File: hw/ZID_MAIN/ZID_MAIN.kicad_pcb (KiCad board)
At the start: 2 copper layers, 144 parts, among them J1 Conn_01x02_Pin_2.54mm, J10 USB-C PWR ONLY, J2 Conn_02x05_2.54mm, J3 Conn_02x05_2.54mm, J4 Conn_02x05_PINHDR_2.54mm, J5 HDR 1x04 Socket, J6 Conn_02x03_Odd_Even, J7 Conn_01x03, J8 BRK EXP SOCKET, J9 Z80-TARGET, M1 WS-RP2040-Zero, SW1 SW_Push, SW2 SW_DIP_x02, U1 74HCT161, U10 74FCT2245, U11 SST39SF010, U12 AS7C1024B-10J, U13 74FCT541C, U14 74AHCT244, U15 74FCT257T, U16 74HCT166, U17 74HCT166, U18 74LVC245, U19 74LVC125AS, U2 74FCT541C, U20 24LC32, U21 ATF1504AS-44T, U22 74AHCT1G125, U23 74LVC273, U24 74AHCT125, U25 74LVC2G04, U3 74FCT541C, U4 MIC2775, U5 OSC-20MHz, U6 Z80 C20MHz-PLCC, U7 ATF1508AS, U8 74FCT2245, U9 74FCT2245

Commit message: Break exp conn 2x20
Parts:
- added TP7: TestPoint, Connector_PinHeader_2.54mm:PinHeader_1x01_P2.54mm_Vertical, F.Cu at (206.4, -30.0)
- added TP8: TestPoint, Connector_PinHeader_2.54mm:PinHeader_1x01_P2.54mm_Vertical, F.Cu at (206.4, -25.4)
- C34: value 220uF -> 100uF; footprint Capacitor_THT:CP_Radial_D6.3mm_P2.50mm -> Capacitor_SMD:C_1210_3225Metric_Pad1.33x2.70mm_HandSolder
- D12: footprint AES_Library:DO-214AB-AES -> Diode_SMD:D_SOD-523
- J2, J3: footprint Connector_PinHeader_2.54mm:PinHeader_2x05_P2.54mm_Vertical -> AES_Library:PinHeader_2x05_AB-AES
- J8: value BRK EXP SOCKET -> BRK-EXP-UNIT; footprint Connector_PinSocket_2.54mm:PinSocket_1x28_P2.54mm_Vertical -> Connector_PinHeader_2.54mm:PinHeader_2x20_P2.54mm_Vertical
- U25: value 74LVC2G04 -> 74LVC3G04; footprint Package_TO_SOT_SMD:SOT-23-6 -> Package_SO:SSOP-8_2.95x2.8mm_P0.65mm
- moved R6 462.4 mm to (-65.1, -39.4)
- moved R7 462.4 mm to (-60.7, -54.1)
- moved R27 460.9 mm to (-41.0, 43.7)
- moved R28 460.7 mm to (-41.0, 48.8)
- moved R29 460.3 mm to (-40.8, 53.8)
- moved R30 460.1 mm to (-40.8, 58.9)
- moved R14 459.7 mm to (-53.6, -50.8)
- moved R15 459.7 mm to (-53.6, -47.9)
- moved R16 459.7 mm to (-53.6, -44.9)
- moved R18 459.7 mm to (-53.6, -39.0)
- moved U19 453.0 mm to (-73.1, -6.99)
- moved U24 445.5 mm to (-34.5, 54.4), turned to 180 degrees
- moved R26 443.6 mm to (-28.0, 52.3)
- moved R25 442.9 mm to (-28.0, 56.9)
- moved D4 437.6 mm to (-46.3, 56.4), turned to -90 degrees
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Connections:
- D10 pad 2: TRST- -> ZBACK-
- D11 pad 1: ZRFSH- -> TRST-
- D11 pad 2: ZBACK- -> ZRFSH-
- J8 pad 1: GND -> LA1
- J8 pad 10: AEN_CLR- -> LA8
- J8 pad 11: BRKHW_DET- -> LA11
- J8 pad 12: BRK2N_AEQ- -> LA10
- J8 pad 13: LA0 -> LA13
- J8 pad 14: LA1 -> LA12
- J8 pad 15: LA2 -> LA15
- J8 pad 16: LA3 -> LA14
- J8 pad 17: LA4 -> BA_CLK
- J8 pad 18: LA5 -> D7_B
- J8 pad 19: LA6 -> BA_CLR-
- J8 pad 2: +5V -> LA0
- J8 pad 20: LA7 -> unconnected-(J8-ADDO1-Pad20)
- J8 pad 21: LA8 -> AEN_CLK
- J8 pad 22: LA9 -> unconnected-(J8-ADDI2-Pad22)
- J8 pad 23: LA10 -> AEN_CLR-
- J8 pad 24: LA11 -> unconnected-(J8-ADDO2-Pad24)
- J8 pad 25: LA12 -> BRKHW_DET-
- J8 pad 26: LA13 -> unconnected-(J8-ADDI3-Pad26)
- J8 pad 27: LA14 -> BRK2N_AEQ-
- J8 pad 28: LA15 -> unconnected-(J8-ADDO3-Pad28)
- J8 pad 3: D7_B -> LA3
- J8 pad 4: unconnected-(J8-ADDR_DOUT-Pad4) -> LA2
- J8 pad 5: BA_CLK -> LA5
- J8 pad 6: BA_CLR- -> LA4
- J8 pad 7: D7_B -> LA7
- J8 pad 8: unconnected-(J8-AEN_DOUT-Pad8) -> LA6
- J8 pad 9: AEN_CLK -> LA9
- RN1 pad 3: /Main Logic/ZA9 -> /Main Logic/ZA10
- RN1 pad 4: /Main Logic/ZA10 -> /Main Logic/ZA9
- RN1 pad 6: /Main Logic/ZA12 -> /Main Logic/ZA13
- RN1 pad 7: /Main Logic/ZA13 -> /Main Logic/ZA12
- RN1 pad 8: /Main Logic/ZA14 -> /Main Logic/ZA15
- RN1 pad 9: /Main Logic/ZA15 -> /Main Logic/ZA14
- U14 pad 1: /Main Logic/BUSACK_L- -> ZBACK-
- U15 pad 15: /Main Logic/BUSACK_H -> /Main Logic/BUSACK
- U25 pad 2: GND -> /Main Logic/BUSACK
- U25 pad 4: /Main Logic/SPICS2- -> GND
- U25 pad 5: +3.3V -> /Main Logic/SPICS2-
- U25 pad 6: /Main Logic/MINT- -> ZBACK-
- U7 pad 1: /Main Logic/BUSACK_H -> /Main Logic/IO1
- U7 pad 2: /Main Logic/BUSACK_L- -> /Main Logic/IO2
- U8 pad 1: /Main Logic/BUSACK_L- -> ZBACK-
- U9 pad 1: /Main Logic/BUSACK_L- -> ZBACK-

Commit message: PCB comp place #1
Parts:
- JP2: value Jumper_2_Small_Open -> Jumper_2_Small_Open_wsto-AES; footprint Connector_PinHeader_2.00mm:PinHeader_1x02_P2.00mm_Vertical -> Connector_PinHeader_2.00mm:PinHeader_1x03_P2.00mm_Vertical
- moved J8 280.7 mm to (233.9, 26.7), turned to -90 degrees
- moved U12 238.6 mm to (125.0, 76.2)
- moved U11 233.5 mm to (142.2, 67.3)
- moved U2 220.3 mm to (175.9, 34.9), turned to 180 degrees
- moved D5 215.9 mm to (106.0, 119.3), turned to -90 degrees
- moved D6 215.5 mm to (109.0, 119.3), turned to -90 degrees
- moved D7 215.3 mm to (112.0, 119.3), turned to -90 degrees
- moved D8 215.1 mm to (115.1, 119.3), turned to -90 degrees
- moved D9 215.0 mm to (118.1, 119.3), turned to -90 degrees
- moved U10 213.9 mm to (213.8, 88.3), turned to 0 degrees
- moved C15 208.6 mm to (217.5, 144.8)
- moved C17 208.6 mm to (217.5, 149.8)
- moved C19 208.6 mm to (221.5, 134.8)
- moved C21 208.6 mm to (221.5, 139.8)
- moved C23 208.6 mm to (221.5, 144.8)
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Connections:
- JP1 pad 1: TRST- -> unconnected-(JP1-A-Pad1)
- JP1 pad 3: unconnected-(JP1-C-Pad3) -> TRST-
- JP2 pad 1: /Main Logic/_CLK -> unconnected-(JP2-A-Pad1)
- JP2 pad 2: /Main Logic/TCLK -> /Main Logic/_CLK
- RN1 pad 3: /Main Logic/ZA10 -> /Main Logic/ZA9
- RN1 pad 4: /Main Logic/ZA9 -> /Main Logic/ZA10
- RN1 pad 6: /Main Logic/ZA13 -> /Main Logic/ZA12
- RN1 pad 7: /Main Logic/ZA12 -> /Main Logic/ZA13
- RN1 pad 8: /Main Logic/ZA15 -> /Main Logic/ZA14
- RN1 pad 9: /Main Logic/ZA14 -> /Main Logic/ZA15
- U8 pad 11: TA7 -> TA0
- U8 pad 12: TA6 -> TA1
- U8 pad 13: TA5 -> TA2
- U8 pad 14: TA4 -> TA3
- U8 pad 15: TA3 -> TA4
- U8 pad 16: TA2 -> TA5
- U8 pad 17: TA1 -> TA6
- U8 pad 18: TA0 -> TA7
- U8 pad 2: /Main Logic/ZA0 -> /Main Logic/ZA7
- U8 pad 3: /Main Logic/ZA1 -> /Main Logic/ZA6
- U8 pad 4: /Main Logic/ZA2 -> /Main Logic/ZA5
- U8 pad 5: /Main Logic/ZA3 -> /Main Logic/ZA4
- U8 pad 6: /Main Logic/ZA4 -> /Main Logic/ZA3
- U8 pad 7: /Main Logic/ZA5 -> /Main Logic/ZA2
- U8 pad 8: /Main Logic/ZA6 -> /Main Logic/ZA1
- U8 pad 9: /Main Logic/ZA7 -> /Main Logic/ZA0
- U9 pad 11: TA15 -> TA8
- U9 pad 12: TA14 -> TA9
- U9 pad 13: TA13 -> TA10
- U9 pad 14: TA12 -> TA11
- U9 pad 15: TA11 -> TA12
- U9 pad 16: TA10 -> TA13
- U9 pad 17: TA9 -> TA14
- U9 pad 18: TA8 -> TA15
- U9 pad 2: /Main Logic/ZA8 -> /Main Logic/ZA15
- U9 pad 3: /Main Logic/ZA9 -> /Main Logic/ZA14
- U9 pad 4: /Main Logic/ZA10 -> /Main Logic/ZA13
- U9 pad 5: /Main Logic/ZA11 -> /Main Logic/ZA12
- U9 pad 6: /Main Logic/ZA12 -> /Main Logic/ZA11
- U9 pad 7: /Main Logic/ZA13 -> /Main Logic/ZA10
- U9 pad 8: /Main Logic/ZA14 -> /Main Logic/ZA9
- U9 pad 9: /Main Logic/ZA15 -> /Main Logic/ZA8

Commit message: PCB layout 2
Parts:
- removed D1: LED BLUE, LED_THT:LED_D3.0mm
- removed D2: LED YELLOW, LED_THT:LED_D3.0mm
- removed D3: LED RED, LED_THT:LED_D3.0mm
- removed D4: LED ORANGE, LED_THT:LED_D3.0mm
- removed D5, D7: LED GREEN, LED_SMD:LED_0805_2012Metric_Pad1.15x1.40mm_HandSolder
- removed D6, D8: LED YELLOW, LED_SMD:LED_0805_2012Metric_Pad1.15x1.40mm_HandSolder
- removed D9: LED RED, LED_SMD:LED_0805_2012Metric_Pad1.15x1.40mm_HandSolder
- added LED1: LED BLUE, LED_THT:LED_D3.0mm, F.Cu at (233.7, 110.2)
- added LED10: LED ORANGE, LED_THT:LED_D3.0mm, F.Cu at (233.7, 115.3)
- added LED2: LED YELLOW, LED_THT:LED_D3.0mm, F.Cu at (233.7, 105.1)
- added LED3: LED RED, LED_THT:LED_D3.0mm, F.Cu at (233.7, 100.1)
- added LED4: LED ORANGE, LED_THT:LED_D3.0mm, F.Cu at (233.7, 95.0)
- added LED5: LED GREEN, LED_SMD:LED_0805_2012Metric_Pad1.15x1.40mm_HandSolder, F.Cu at (74.5, 97.0)
- added LED6: LED GREEN, LED_SMD:LED_0805_2012Metric_Pad1.15x1.40mm_HandSolder, F.Cu at (74.5, 100.1)
- added LED7: LED YELLOW, LED_SMD:LED_0805_2012Metric_Pad1.15x1.40mm_HandSolder, F.Cu at (74.5, 103.1)
- added LED8: LED YELLOW, LED_SMD:LED_0805_2012Metric_Pad1.15x1.40mm_HandSolder, F.Cu at (74.5, 106.1)
- added LED9: LED RED, LED_SMD:LED_0805_2012Metric_Pad1.15x1.40mm_HandSolder, F.Cu at (74.5, 109.2)
- added R37: 1.2k, Resistor_SMD:R_0805_2012Metric, F.Cu at (224.1, 112.0)
- added U26: 74AHCT1G14, Package_TO_SOT_SMD:SOT-23-5, F.Cu at (217.6, 41.8)
- U25: value 74LVC3G04 -> 74LVC2G04; footprint Package_SO:SSOP-8_2.95x2.8mm_P0.65mm -> Package_TO_SOT_SMD:SOT-23-6
- moved TP1 158.7 mm to (233.0, 119.4)
- moved R27 145.3 mm to (224.0, 109.1), turned to 180 degrees
- moved R30 144.6 mm to (224.0, 93.9), turned to 180 degrees
- moved R28 144.5 mm to (224.0, 104.0), turned to 180 degrees
- moved R29 144.1 mm to (224.0, 98.9), turned to 180 degrees
- moved R17 142.3 mm to (223.6, 114.6), turned to 180 degrees
- moved R26 134.9 mm to (218.8, 105.9), turned to -90 degrees
- moved U22 129.3 mm to (214.9, 112.5), turned to 0 degrees
- moved U24 127.5 mm to (215.2, 98.0), turned to 0 degrees
- moved R25 125.0 mm to (212.0, 105.9), turned to -90 degrees
- moved SPARE1 113.3 mm to (111.8, 93.5)
- moved C17 98.7 mm to (244.8, 55.0)
- moved C25 98.7 mm to (248.8, 55.0)
- moved C30 98.7 mm to (252.8, 47.5)
- moved C33 98.7 mm to (252.8, 55.0)
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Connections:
- RN1 pad 2: /Main Logic/ZA8 -> /Main Logic/ZA12
- RN1 pad 3: /Main Logic/ZA9 -> /Main Logic/ZA11
- RN1 pad 5: /Main Logic/ZA11 -> /Main Logic/ZA9
- RN1 pad 6: /Main Logic/ZA12 -> /Main Logic/ZA13
- RN1 pad 7: /Main Logic/ZA13 -> /Main Logic/ZA8
- U25 pad 2: /Main Logic/BUSACK -> GND
- U25 pad 4: GND -> /Main Logic/SPICS2-
- U25 pad 5: /Main Logic/SPICS2- -> +3.3V
- U25 pad 6: ZBACK- -> /Main Logic/MINT-

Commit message: PCB-Main layout 3
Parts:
- moved TP8 17.0 mm to (157.5, 61.7)
- moved TP7 17.0 mm to (157.5, 69.1)
- moved J2 3.46 mm to (231.7, 44.1)
- moved J3 3.46 mm to (231.7, 31.4)
- moved J9 3.46 mm to (231.7, 72.7)
- moved LED1 3.46 mm to (233.7, 106.7)
- moved LED10 3.46 mm to (233.7, 111.9)
- moved LED2 3.46 mm to (233.7, 101.7)
- moved LED3 3.46 mm to (233.7, 96.6)
- moved LED4 3.46 mm to (233.7, 91.5)
- moved R21 3.30 mm to (216.2, 61.0)
- moved J8 3.12 mm to (211.1, 26.7)
- moved R20 3.12 mm to (176.8, 34.5)
- moved R19 3.12 mm to (179.4, 34.5)
- moved TP1 2.56 mm to (233.7, 116.9)
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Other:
- board outline added: 165.1 x 101.6 mm

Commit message: PCB Main: layout 20250411a
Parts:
- added J11: Conn_01x08, Connector_PinHeader_2.54mm:PinHeader_1x08_P2.54mm_Vertical, F.Cu at (215.6, 83.8)
- LED5, LED6, LED7, LED8, LED9: footprint LED_SMD:LED_0805_2012Metric_Pad1.15x1.40mm_HandSolder -> LED_THT:LED_D3.0mm
- moved SW1 179.5 mm to (232.1, 29.2), turned to -90 degrees
- moved J1 149.8 mm to (218.8, 34.3), turned to 90 degrees
- moved U4 137.8 mm to (212.5, 34.6), turned to 0 degrees
- moved U22 25.2 mm to (223.8, 88.9)
- moved TP1 22.3 mm to (234.0, 94.6)
- moved R17 20.8 mm to (226.4, 94.0)
- moved R26 12.7 mm to (216.1, 118.4)
- moved R25 12.4 mm to (212.3, 118.4)
- moved U24 12.4 mm to (215.5, 110.5)
- moved R33 11.8 mm to (81.0, 111.8)
- moved LED1 10.1 mm to (233.7, 116.8)
- moved LED10 10.1 mm to (233.7, 121.9)
- moved LED2 10.1 mm to (233.7, 111.7)
- moved LED3 10.1 mm to (233.7, 106.7)
- moved LED4 10.1 mm to (233.7, 101.6)
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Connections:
- J1 pad 1: Net-(J1-Pin_1) -> GND
- J1 pad 2: GND -> Net-(J1-Pin_2)
- J8 pad 28: unconnected-(J8-ADDO3-Pad28) -> D7_B
- J8 pad 29: +5V -> TM1-
- J8 pad 30: D7_B -> unconnected-(J8-AEDO1-Pad30)
- J8 pad 31: +5V -> TMREQ-
- J8 pad 33: +5V -> TIORQ-
- J8 pad 35: GND -> TWR-
- J8 pad 37: GND -> TRD-
- J8 pad 38: unconnected-(J8-AEDI3-Pad38) -> GND
- J8 pad 40: unconnected-(J8-AEDO3-Pad40) -> +5V
- SW1 pad 2: Net-(J1-Pin_1) -> Net-(J1-Pin_2)
- U4 pad 4: Net-(J1-Pin_1) -> Net-(J1-Pin_2)
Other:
- outline, holes or cut-outs redrawn

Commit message: POD-1 pcb
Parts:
- moved JP1 31.1 mm to (168.0, 115.6)
- moved JP2 31.1 mm to (162.9, 115.6)
- moved SBC1 5.17 mm to (147.1, 115.6)
- moved SBC3 5.17 mm to (157.2, 115.6)
- moved SBC2 5.17 mm to (152.1, 115.6)
- moved R4 3.36 mm to (157.2, 111.5)
- moved J1 2.62 mm to (221.3, 34.9)
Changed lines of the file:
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@@
 	(footprint "Connector_PinHeader_2.00mm:PinHeader_1x03_P2.00mm_Vertical"
 		(layer "F.Cu")
-		(at 152.146 114.586)
+		(at 157.226 115.57)
 		(descr "Through hole straight pin header, 1x03, 2.00mm pitch, single row")
 		(tags "Through hole pin header THT 1x03 2.00mm single row")
@@
 	(footprint "Connector_PinHeader_2.54mm:PinHeader_1x02_P2.54mm_Vertical"
 		(layer "F.Cu")
-		(at 218.75112 34.29 90)
+		(at 221.29612 34.925 90)
 		(descr "Through hole straight pin header, 1x02, 2.54mm pitch, single row")
 		(tags "Through hole pin header THT 1x02 2.54mm single row")
 		(property "Reference" "J1"
-			(at -0.889 5.085 90)
+			(at 2.54 -0.635 180)
 			(layer "F.SilkS")
 			(effects
@@
 	(footprint "Connector_PinHeader_2.00mm:PinHeader_1x03_P2.00mm_Vertical"
 		(layer "F.Cu")
-		(at 131.826 114.586)
+		(at 162.87612 115.57)
 		(descr "Through hole straight pin header, 1x03, 2.00mm pitch, single row")
 		(tags "Through hole pin header THT 1x03 2.00mm single row")
@@
 	(footprint "Connector_PinHeader_2.00mm:PinHeader_1x03_P2.00mm_Vertical"
 		(layer "F.Cu")
-		(at 141.986 114.586)
+		(at 147.066 115.57)
 		(descr "Through hole straight pin header, 1x03, 2.00mm pitch, single row")
 		(tags "Through hole pin header THT 1x03 2.00mm single row")
@@
 	(footprint "Resistor_SMD:R_0805_2012Metric"
 		(layer "F.Cu")
-		(at 156.718 114.808 90)
+		(at 157.16112 111.474 90)
 		(descr "Resistor SMD 0805 (2012 Metric), square (rectangular) end terminal, IPC-7351 nominal, (Body size source: IPC-SM-782 page 72, https://www.pcb-3d.com/wordpress/wp-content/uploads/ipc-sm-782a_amendment_1_and_2.pdf), generated with kicad-footprint-generator")
 		(tags "resistor")
@@
 	(footprint "Connector_PinHeader_2.00mm:PinHeader_1x03_P2.00mm_Vertical"
 		(layer "F.Cu")
-		(at 136.906 114.586)
+		(at 167.95612 115.57)
 		(descr "Through hole straight pin header, 1x03, 2.00mm pitch, single row")
 		(tags "Through hole pin header THT 1x03 2.00mm single row")
@@
 	(footprint "Connector_PinHeader_2.00mm:PinHeader_1x03_P2.00mm_Vertical"
 		(layer "F.Cu")
-		(at 147.066 114.586)
+		(at 152.146 115.57)
 		(descr "Through hole straight pin header, 1x03, 2.00mm pitch, single row")
 		(tags "Through hole pin header THT 1x03 2.00mm single row")
@@
 		(tags "Tactile Switch")
 		(property "Reference" "SW1"
-			(at 5.08 5.08 0)
+			(at 4.445 4.445 90)
 			(layer "F.SilkS")
 			(effects

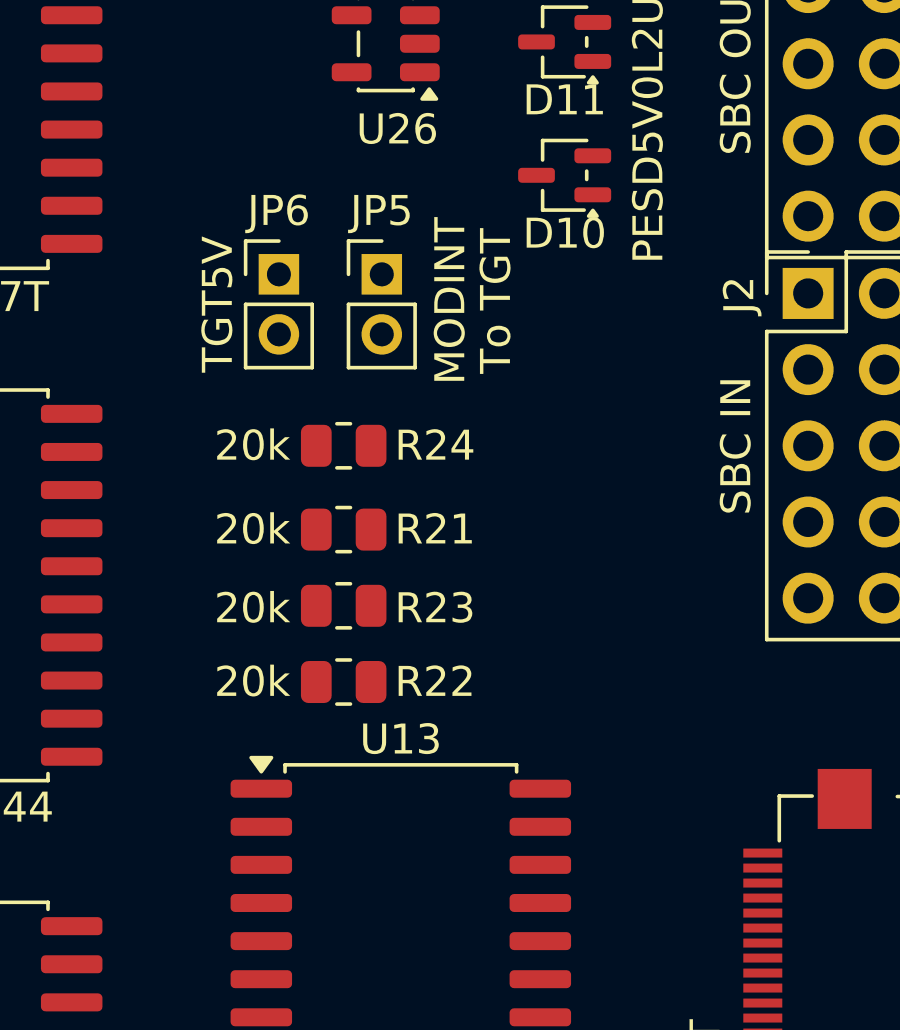
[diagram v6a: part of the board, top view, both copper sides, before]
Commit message: POD PCB increase GND trace width
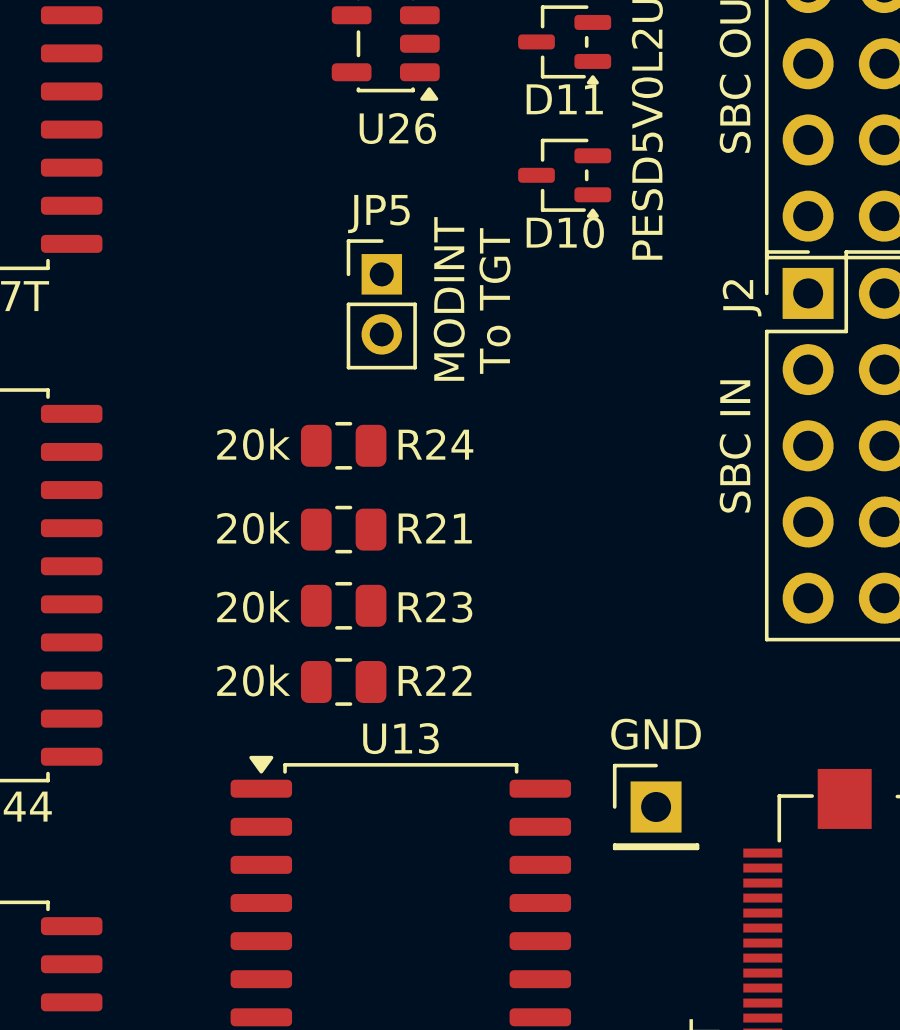
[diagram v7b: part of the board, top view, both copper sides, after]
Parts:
- removed JP6: Jumper_2_Small_Open, Connector_PinHeader_2.00mm:PinHeader_1x02_P2.00mm_Vertical
- added TP9: TestPoint, Connector_PinHeader_2.54mm:PinHeader_1x01_P2.54mm_Vertical, F.Cu at (226.6, 67.3)
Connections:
- J9 pad 11: Net-(J9-5V) -> GND
